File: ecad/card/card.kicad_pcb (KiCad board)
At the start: 4 copper layers, 133.4 x 32.2 mm, 136 parts, among them J1 Conn_01x03_Pin, J2 USB4105-GF-A, J3 10145226-0241N13LF, J4 Conn_01x03_Pin, J5 Conn_01x03_Pin, SW1 SW_Push, SW2 SW_Push, U1 W25Q128JVS, U2 RP2350_80QFN, U3 MCP23017_SO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

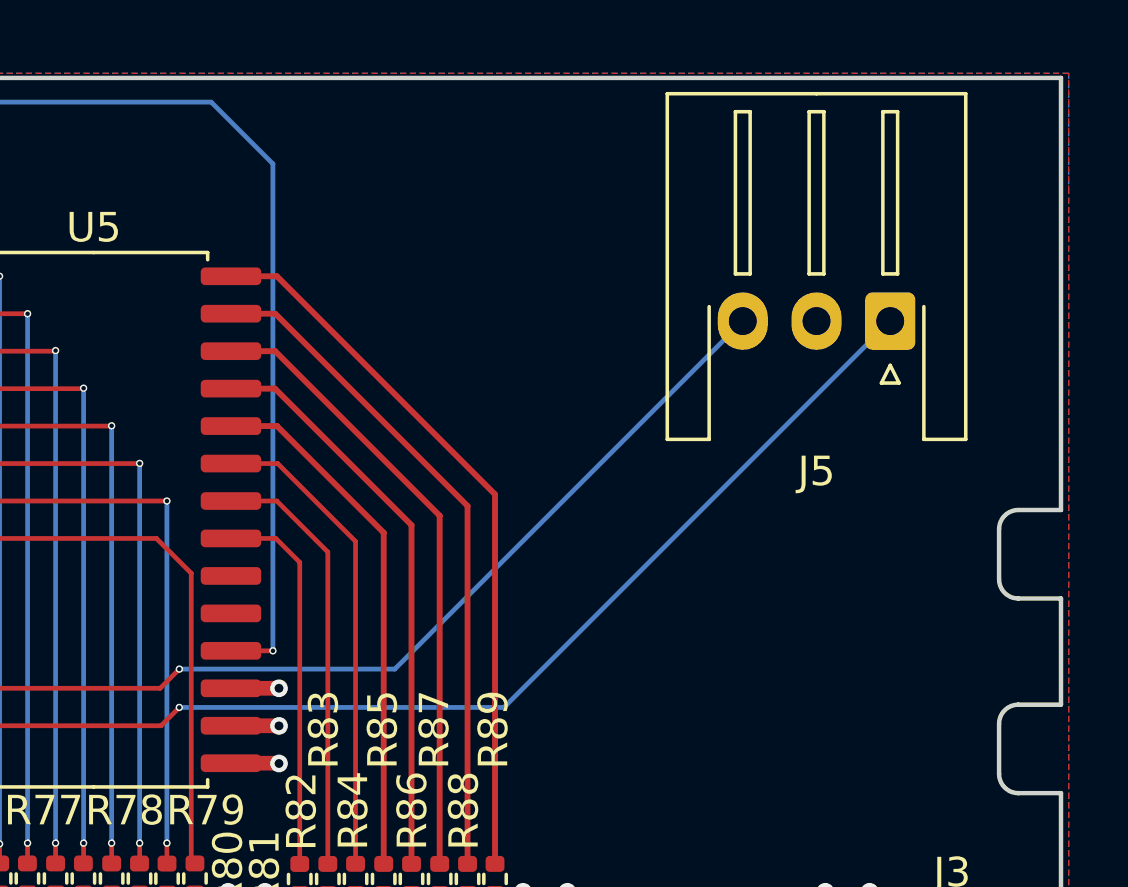
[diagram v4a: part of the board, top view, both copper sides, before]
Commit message: rotate card UART 90
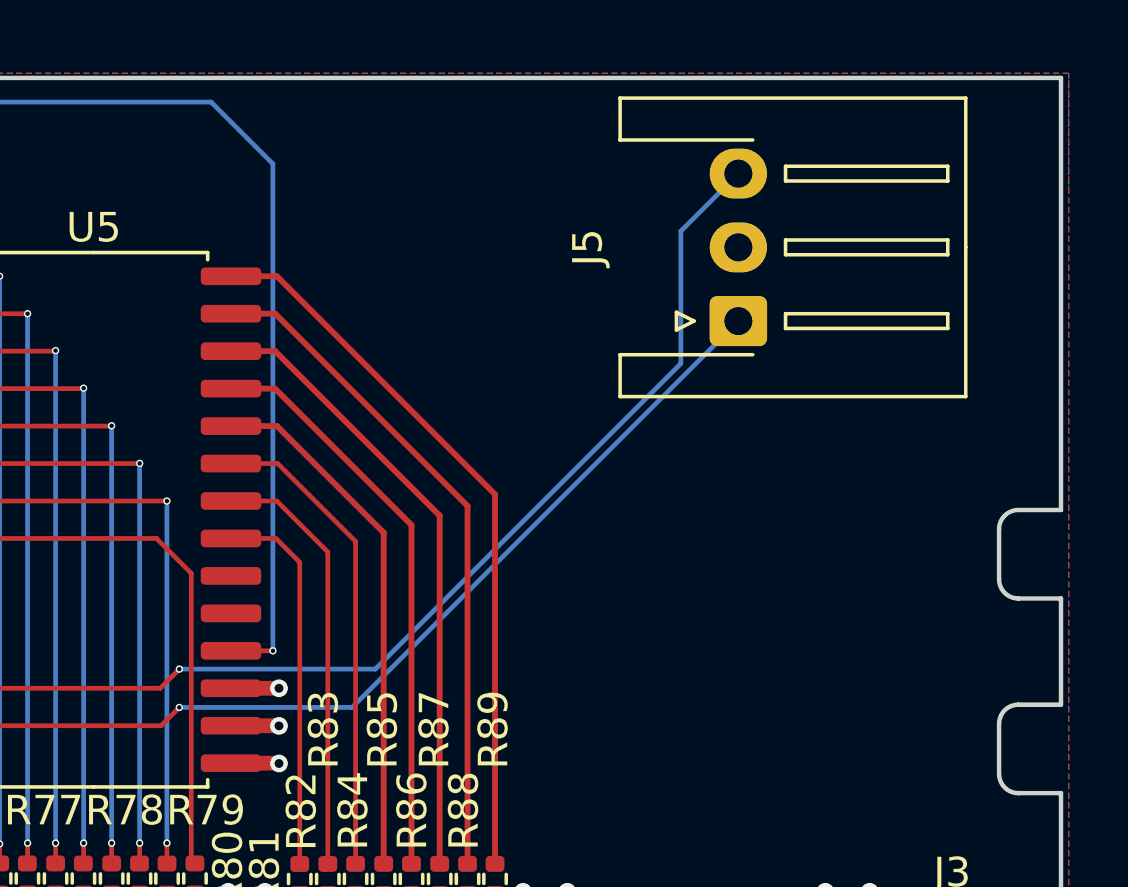
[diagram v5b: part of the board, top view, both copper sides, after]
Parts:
- moved J5 5.15 mm to (172.6, 57.4), turned to 90 degrees
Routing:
- net /I2C1_SDA: track 70.3 -> 65.1 mm
- net /I2C1_SCL: track 66.2 -> 70.7 mm
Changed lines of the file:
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@@
 	(footprint "Connector_JST:JST_XH_S3B-XH-A-1_1x03_P2.50mm_Horizontal"
 		(layer "F.Cu")
-		(at 177.7 57.4 180)
+		(at 172.55 57.4 90)
 		(descr "JST XH series connector, S3B-XH-A-1 (http://www.jst-mfg.com/product/pdf/eng/eXH.pdf), generated with kicad-footprint-generator")
 		(tags "connector JST XH horizontal")
 		(property "Reference" "J5"
-			(at 2.5 -5.1 0)
+			(at 2.5 -5.1 90)
 			(layer "F.SilkS")
 			(effects
@@
 		)
 		(property "Value" "Conn_01x03_Pin"
-			(at 2.5 8.8 0)
+			(at 2.5 8.8 90)
 			(layer "F.Fab")
 			(effects
@@
 		)
 		(property "Footprint" "Connector_JST:JST_XH_S3B-XH-A-1_1x03_P2.50mm_Horizontal"
-			(at 0 0 180)
+			(at 0 0 90)
 			(unlocked yes)
 			(layer "F.Fab")
@@
 		)
 		(property "Datasheet" ""
-			(at 0 0 180)
+			(at 0 0 90)
 			(unlocked yes)
 			(layer "F.Fab")
@@
 		)
 		(property "Description" "Generic connector, single row, 01x03, script generated"
-			(at 0 0 180)
+			(at 0 0 90)
 			(unlocked yes)
 			(layer "F.Fab")
@@
 		(attr through_hole)
 		(fp_line
-			(start 7.56 7.71)
-			(end 7.56 -4.01)
-			(stroke
-				(width 0.12)
-				(type solid)
-			)
-			(layer "F.SilkS")
-		)
-		(fp_line
 			(start 7.56 -4.01)
 			(end 6.14 -4.01)
@@
 		)
 		(fp_line
-			(start 5.25 7.1)
-			(end 5.25 1.6)
+			(start -1.14 -4.01)
+			(end -1.14 0.49)
 			(stroke
 				(width 0.12)
@@
 		)
 		(fp_line
-			(start 5.25 1.6)
-			(end 4.75 1.6)
+			(start -2.56 -4.01)
+			(end -1.14 -4.01)
 			(stroke
 				(width 0.12)
@@
 		)
 		(fp_line
-			(start 4.75 7.1)
-			(end 5.25 7.1)
+			(start 0.3 -2.1)
+			(end 0 -1.5)
 			(stroke
 				(width 0.12)
@@
 		)
 		(fp_line
-			(start 4.75 1.6)
-			(end 4.75 7.1)
+			(start -0.3 -2.1)
+			(end 0.3 -2.1)
 			(stroke
 				(width 0.12)
@@
 		)
 		(fp_line
-			(start 2.75 7.1)
-			(end 2.75 1.6)
+			(start 0 -1.5)
+			(end -0.3 -2.1)
 			(stroke
 				(width 0.12)
@@
 		)
 		(fp_line
-			(start 2.75 1.6)
-			(end 2.25 1.6)
+			(start 5.25 1.6)
+			(end 4.75 1.6)
 			(stroke
 				(width 0.12)
@@
 		)
 		(fp_line
-			(start 2.5 7.71)
-			(end 7.56 7.71)
+			(start 4.75 1.6)
+			(end 4.75 7.1)
 			(stroke
 				(width 0.12)
@@
 		)
 		(fp_line
-			(start 2.5 7.71)
-			(end -2.56 7.71)
+			(start 2.75 1.6)
+			(end 2.25 1.6)
 			(stroke
 				(width 0.12)
@@
 		)
 		(fp_line
-			(start 2.25 7.1)
-			(end 2.75 7.1)
+			(start 2.25 1.6)
+			(end 2.25 7.1)
 			(stroke
 				(width 0.12)
@@
 		)
 		(fp_line
-			(start 2.25 1.6)
-			(end 2.25 7.1)
+			(start 0.25 1.6)
+			(end -0.25 1.6)
 			(stroke
 				(width 0.12)
@@
 		)
 		(fp_line
-			(start 0.3 -2.1)
-			(end 0 -1.5)
+			(start -0.25 1.6)
+			(end -0.25 7.1)
 			(stroke
 				(width 0.12)
@@
 		)
 		(fp_line
-			(start 0.25 7.1)
-			(end 0.25 1.6)
+			(start 5.25 7.1)
+			(end 5.25 1.6)
 			(stroke
 				(width 0.12)
@@
 		)
 		(fp_line
-			(start 0.25 1.6)
-			(end -0.25 1.6)
+			(start 4.75 7.1)
+			(end 5.25 7.1)
 			(stroke
 				(width 0.12)
@@
 		)
 		(fp_line
-			(start 0 -1.5)
-			(end -0.3 -2.1)
+			(start 2.75 7.1)
+			(end 2.75 1.6)
 			(stroke
 				(width 0.12)
@@
 		)
 		(fp_line
-			(start -0.25 7.1)
-			(end 0.25 7.1)
+			(start 2.25 7.1)
+			(end 2.75 7.1)
 			(stroke
 				(width 0.12)
@@
 		)
 		(fp_line
-			(start -0.25 1.6)
-			(end -0.25 7.1)
+			(start 0.25 7.1)
+			(end 0.25 1.6)
 			(stroke
 				(width 0.12)
@@
 		)
 		(fp_line
-			(start -0.3 -2.1)
-			(end 0.3 -2.1)
+			(start -0.25 7.1)
+			(end 0.25 7.1)
 			(stroke
 				(width 0.12)
@@
 		)
 		(fp_line
-			(start -1.14 -4.01)
-			(end -1.14 0.49)
+			(start 7.56 7.71)
+			(end 7.56 -4.01)
 			(stroke
 				(width 0.12)
@@
 		)
 		(fp_line
-			(start -2.56 7.71)
-			(end -2.56 -4.01)
+			(start 2.5 7.71)
+			(end 7.56 7.71)
 			(stroke
 				(width 0.12)
@@
 		)
 		(fp_line
-			(start -2.56 -4.01)
-			(end -1.14 -4.01)
+			(start 2.5 7.71)
+			(end -2.56 7.71)
 			(stroke
 				(width 0.12)
@@
 		)
 		(fp_line
-			(start 7.95 8.1)
-			(end 7.95 -4.4)
+			(start -2.56 7.71)
+			(end -2.56 -4.01)
 			(stroke
-				(width 0.05)
+				(width 0.12)
 				(type solid)
 			)
-			(layer "F.CrtYd")
+			(layer "F.SilkS")
 		)
 		(fp_line
@@
 		)
 		(fp_line
-			(start -2.95 8.1)
-			(end 7.95 8.1)
+			(start -2.95 -4.4)
+			(end -2.95 8.1)
 			(stroke
 				(width 0.05)
@@
 		)
 		(fp_line
-			(start -2.95 -4.4)
-			(end -2.95 8.1)
+			(start 7.95 8.1)
+			(end 7.95 -4.4)
 			(stroke
 				(width 0.05)
@@
 		)
 		(fp_line
-			(start 7.45 7.6)
-			(end 7.45 -3.9)
+			(start -2.95 8.1)
+			(end 7.95 8.1)
 			(stroke
-				(width 0.1)
+				(width 0.05)
 				(type solid)
 			)
-			(layer "F.Fab")
+			(layer "F.CrtYd")
 		)
 		(fp_line
@@
 		)
 		(fp_line
-			(start 6.25 0.6)
-			(end 2.5 0.6)
+			(start 6.25 -3.9)
+			(end 6.25 0.6)
 			(stroke
 				(width 0.1)
@@
 		)
 		(fp_line
-			(start 6.25 -3.9)
-			(end 6.25 0.6)
+			(start -1.25 -3.9)
+			(end -1.25 0.6)
 			(stroke
 				(width 0.1)
@@
 		)
 		(fp_line
-			(start 2.5 7.6)
-			(end 7.45 7.6)
+			(start -2.45 -3.9)
+			(end -1.25 -3.9)
 			(stroke
 				(width 0.1)
@@
 		)
 		(fp_line
-			(start 2.5 7.6)
-			(end -2.45 7.6)
+			(start 0 -0.4)
+			(end 0.625 0.6)
 			(stroke
 				(width 0.1)
@@
 		)
 		(fp_line
-			(start 0 -0.4)
-			(end 0.625 0.6)
+			(start 6.25 0.6)
+			(end 2.5 0.6)
 			(stroke
 				(width 0.1)
@@
 		)
 		(fp_line
-			(start -1.25 -3.9)
-			(end -1.25 0.6)
+			(start 7.45 7.6)
+			(end 7.45 -3.9)
 			(stroke
 				(width 0.1)
@@
 		)
 		(fp_line
-			(start -2.45 7.6)
-			(end -2.45 -3.9)
+			(start 2.5 7.6)
+			(end 7.45 7.6)
 			(stroke
 				(width 0.1)
@@
 		)
 		(fp_line
-			(start -2.45 -3.9)
-			(end -1.25 -3.9)
+			(start 2.5 7.6)
+			(end -2.45 7.6)
+			(stroke
+				(width 0.1)
+				(type solid)
+			)
+			(layer "F.Fab")
+		)
+		(fp_line
+			(start -2.45 7.6)
+			(end -2.45 -3.9)
 			(stroke
 				(width 0.1)
@@
 		)
 		(fp_text user "${REFERENCE}"
-			(at 2.5 1.85 0)
+			(at 2.5 1.85 90)
 			(layer "F.Fab")
 			(effects
@@
 		)
 		(pad "1" thru_hole roundrect
-			(at 0 0 180)
+			(at 0 0 90)
 			(size 1.7 1.95)
 			(drill 0.95)
@@
 		)
 		(pad "2" thru_hole oval
-			(at 2.5 0 180)
+			(at 2.5 0 90)
 			(size 1.7 1.95)
 			(drill 0.95)
@@
 		)
 		(pad "3" thru_hole oval
-			(at 5 0 180)
+			(at 5 0 90)
 			(size 1.7 1.95)
 			(drill 0.95)
@@
 	)
 	(gr_text "I2C 1\nUART 1"
-		(at 175.2 50 0)
+		(at 177.5 50.1 0)
 		(layer "B.SilkS" knockout)
 		(effects
@@
 	)
 	(segment
-		(start 160.9 69.2)
-		(end 172.7 57.4)
+		(start 170.6 58.840884)
+		(end 170.6 54.35)
 		(width 0.16)
 		(layer "B.Cu")
@@
 	)
 	(segment
+		(start 160.240884 69.2)
+		(end 170.6 58.840884)
+		(width 0.16)
+		(layer "B.Cu")
+		(net 237)
+	)
+	(segment
 		(start 140.200803 74.276797)
 		(end 144.6276 69.85)
@@
 	(segment
 		(start 153.595 69.2)
-		(end 160.9 69.2)
+		(end 160.240884 69.2)
+		(width 0.16)
+		(layer "B.Cu")
+		(net 237)
+	)
+	(segment
+		(start 170.6 54.35)
+		(end 172.55 52.4)
 		(width 0.16)
 		(layer "B.Cu")
@@
 	)
 	(segment
-		(start 133.301797 74.7268)
-		(end 141.0208 74.7268)
+		(start 159.45 70.5)
+		(end 172.55 57.4)
 		(width 0.16)
 		(layer "B.Cu")
@@
 	)
 	(segment
-		(start 133.3 74.725003)
-		(end 133.301797 74.7268)
+		(start 133.301797 74.7268)
+		(end 141.0208 74.7268)
 		(width 0.16)
 		(layer "B.Cu")
@@
 	)
 	(segment
-		(start 141.0208 74.7268)
-		(end 144.6276 71.12)
+		(start 153.595 70.5)
+		(end 159.45 70.5)
 		(width 0.16)
 		(layer "B.Cu")
@@
 	)
 	(segment
-		(start 164.6 70.5)
-		(end 177.7 57.4)
+		(start 133.3 74.725003)
+		(end 133.301797 74.7268)
 		(width 0.16)
 		(layer "B.Cu")
@@
 	)
 	(segment
-		(start 153.595 70.5)
-		(end 164.6 70.5)
+		(start 141.0208 74.7268)
+		(end 144.6276 71.12)
 		(width 0.16)
 		(layer "B.Cu")
